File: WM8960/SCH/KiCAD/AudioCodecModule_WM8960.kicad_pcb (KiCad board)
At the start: 2 copper layers, 75 x 50 mm, 71 parts, among them J1 Line in right filter, J10 Conn_02x06_Top_Bottom, J2 Line in left filter, J3 Line out left, J4 Line out right, J5 Line in right, J6 Line in left, J7 Conn_01x04, J8 Line out, J9 Line in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

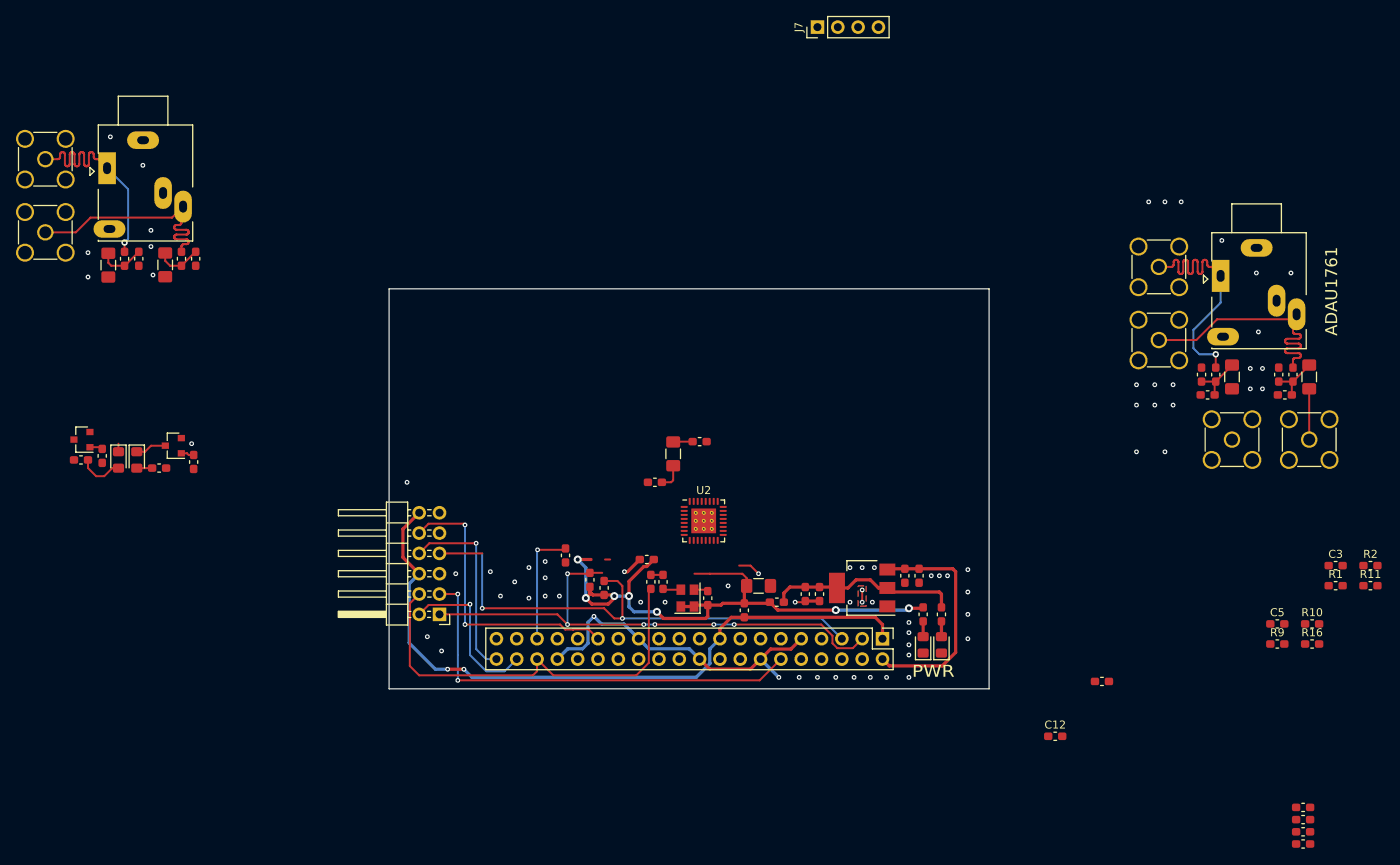
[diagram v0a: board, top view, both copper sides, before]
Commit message: WM8960 CODEC schematic ready
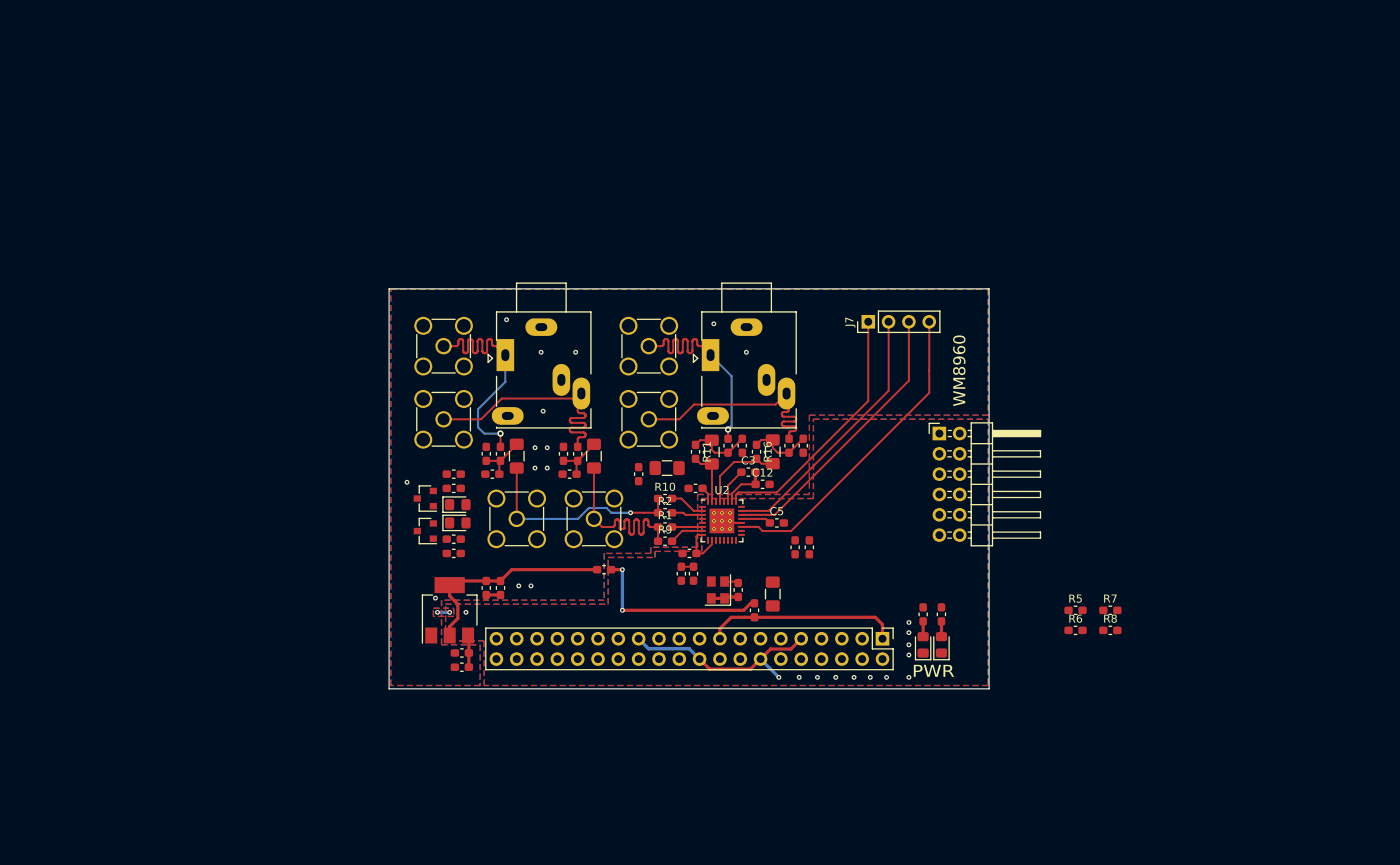
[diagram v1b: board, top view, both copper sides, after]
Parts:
- removed C10: 100n, Capacitor_SMD:C_0603_1608Metric_Pad1.05x0.95mm_HandSolder
- removed C2: 47p, Capacitor_SMD:C_0603_1608Metric_Pad1.05x0.95mm_HandSolder
- moved C14 90.0 mm to (156.0, 71.9)
- moved C15 90.0 mm to (152.1, 71.6)
- moved J1 90.0 mm to (156.0, 79.8)
- moved J9 90.0 mm to (154.4, 59.7)
- moved R12 90.0 mm to (152.9, 74.2)
- moved R21 90.0 mm to (163.6, 71.6)
- moved C19 90.0 mm to (165.6, 71.9)
- moved C20 90.0 mm to (161.8, 71.6)
- moved J2 90.0 mm to (165.6, 79.8)
- moved J5 90.0 mm to (146.8, 67.3)
- moved J6 90.0 mm to (146.8, 58.2)
- moved R14 90.0 mm to (162.6, 74.2)
- moved R22 90.0 mm to (153.9, 71.6)
- moved R2 88.4 mm to (174.5, 79.0)
- moved R11 86.0 mm to (178.3, 71.4), turned to 270 degrees
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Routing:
- net /I2C_SDA: track 66.4 -> 0.00 mm, vias 6 -> 0
- net /I2C_SCL: track 65.5 -> 0.14 mm, vias 2 -> 0
- net /3V3_IN: track 86.5 -> 24.3 mm, vias 2 -> 0
- net /I2S_CLK: track 54.6 -> 0.00 mm, vias 2 -> 0
- net /MCLK_IN: track 54.1 -> 0.00 mm
- net /3V3: track 78.5 -> 32.7 mm, vias 7 -> 2
- net /SPK_RN: track 0.00 -> 39.7 mm
- net /L-BLUE: track 36.1 -> 0.00 mm, vias 2 -> 0
- net /SPK_RP: track 0.00 -> 35.2 mm
- net /SPK_LN: track 0.00 -> 33.2 mm
- net /SPK_LP: track 0.00 -> 32.1 mm
- net Net-(C14-Pad2): track 0.00 -> 26.6 mm, vias 0 -> 1
- net /5V_IN: track 29.0 -> 4.00 mm
- net /I2S_DAC: track 23.9 -> 0.00 mm, vias 1 -> 0
- net /I2S_ADC: track 20.5 -> 0.00 mm, vias 1 -> 0
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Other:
- board text added: "WM8960"
- board text removed: "ADAU1761"

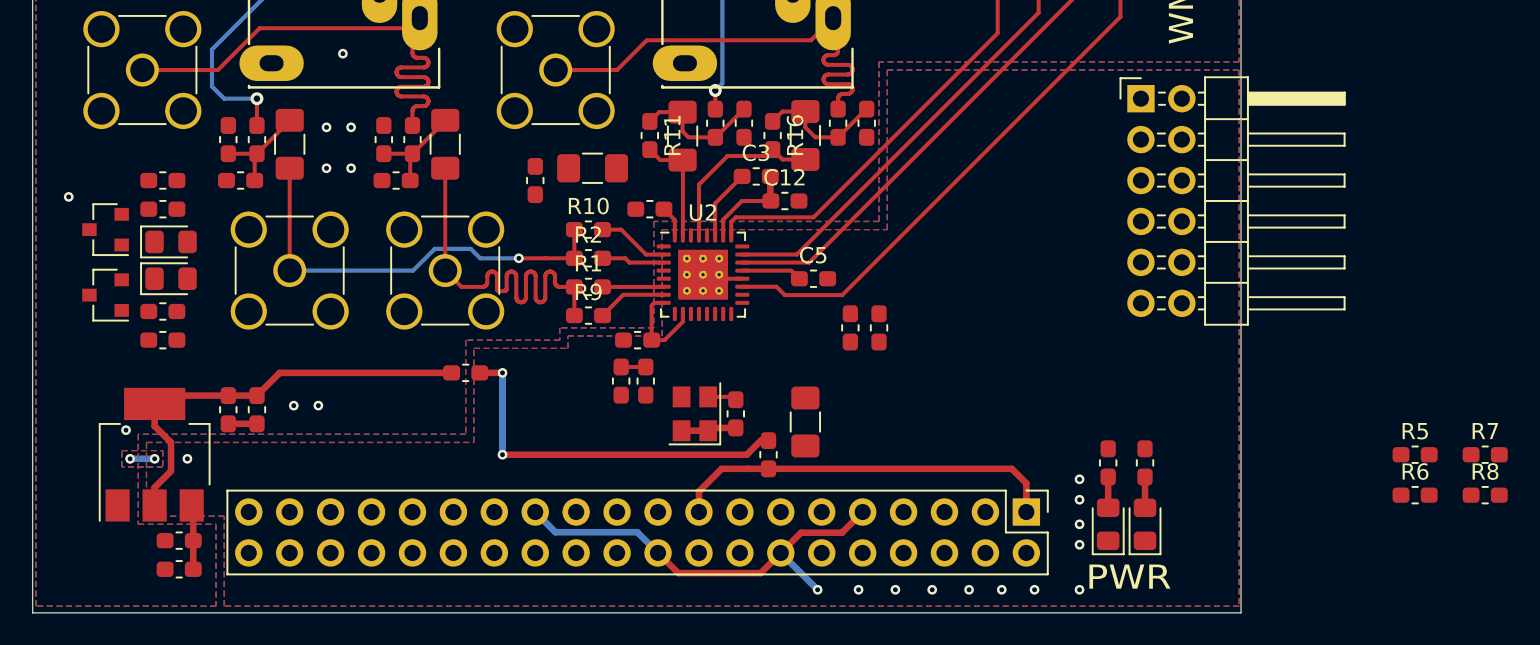
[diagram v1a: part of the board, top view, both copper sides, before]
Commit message: WM8960 PCB added
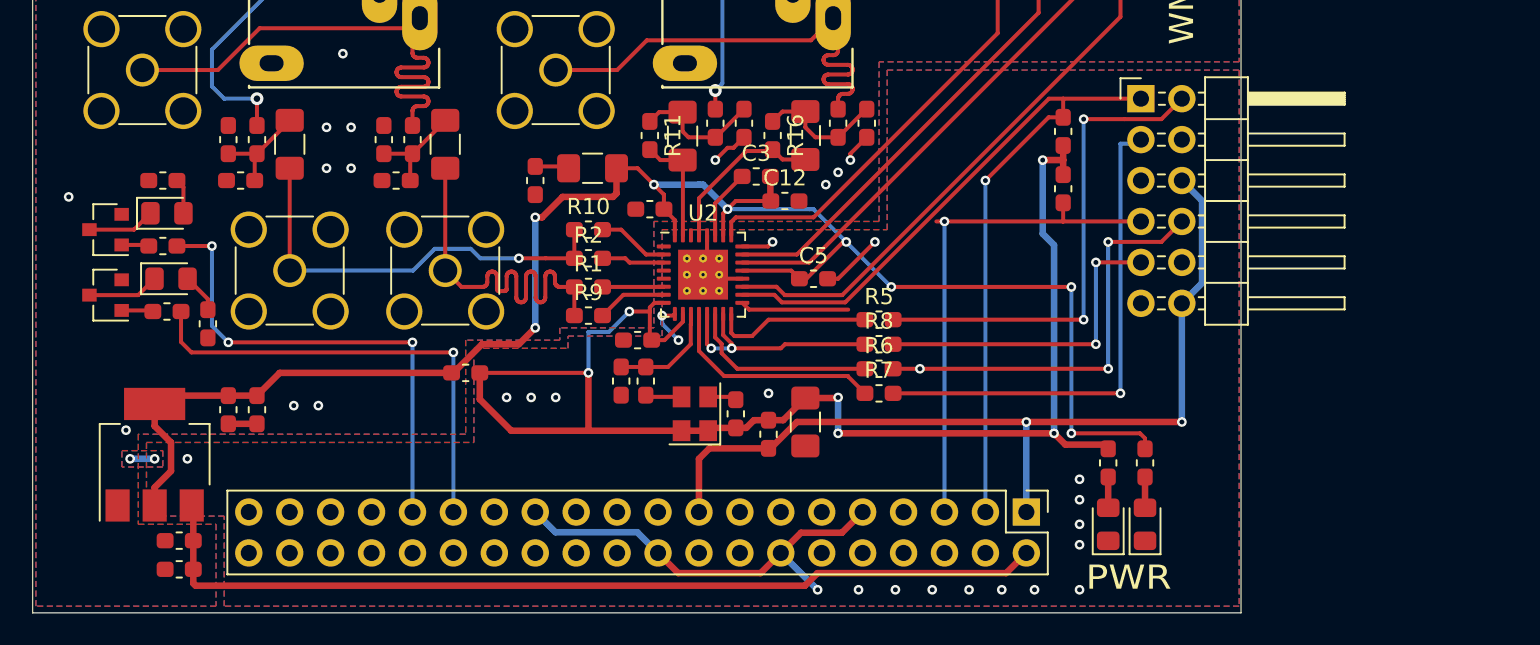
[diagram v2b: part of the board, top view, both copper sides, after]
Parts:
- moved R8 38.8 mm to (192.5, 84.3)
- moved R7 37.8 mm to (192.5, 87.4)
- moved R5 34.3 mm to (192.5, 82.8)
- moved R6 34.2 mm to (192.5, 85.9)
- moved R24 16.7 mm to (204.0, 71.1)
- moved R25 15.8 mm to (204.0, 74.7), turned to 90 degrees
- moved R29 2.97 mm to (150.9, 83.1), turned to 90 degrees
- moved R30 2.29 mm to (148.1, 78.2)
- moved D4 1.80 mm to (148.3, 76.2)
- moved FB1 1.27 mm to (185.7, 89.9)
- moved R28 0.25 mm to (148.3, 82.3)
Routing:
- net /A3V3: track 38.0 -> 110.0 mm, vias 0 -> 8
- net /I2C_SDA: track 0.00 -> 58.4 mm, vias 0 -> 1
- net /3V3: track 32.7 -> 88.4 mm, vias 2 -> 6
- net /5V_IN: track 4.00 -> 57.5 mm
- net /I2C_SCL: track 0.14 -> 38.6 mm, vias 0 -> 1
- net /3V3_IN: track 24.3 -> 55.8 mm, vias 0 -> 2
- net /I2S_CLK: track 0.00 -> 31.0 mm, vias 0 -> 1
- net /I2S_ADC: track 0.00 -> 30.9 mm, vias 0 -> 2
- net /L-GREEN: track 0.00 -> 30.5 mm, vias 0 -> 3
- net /L-BLUE: track 0.00 -> 29.0 mm, vias 0 -> 1
- net /I2S_DAC: track 0.00 -> 26.3 mm, vias 0 -> 3
- net /I2S_RLCLK: track 0.00 -> 20.5 mm, vias 0 -> 2
- net GND: track 33.3 -> 47.8 mm, vias 29 -> 41
- net Net-(R8-Pad1): track 0.00 -> 14.2 mm, vias 0 -> 2
- net Net-(R7-Pad1): track 0.00 -> 13.7 mm
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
